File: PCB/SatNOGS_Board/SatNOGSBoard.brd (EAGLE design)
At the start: 58.1 x 68.6 mm, 13 parts

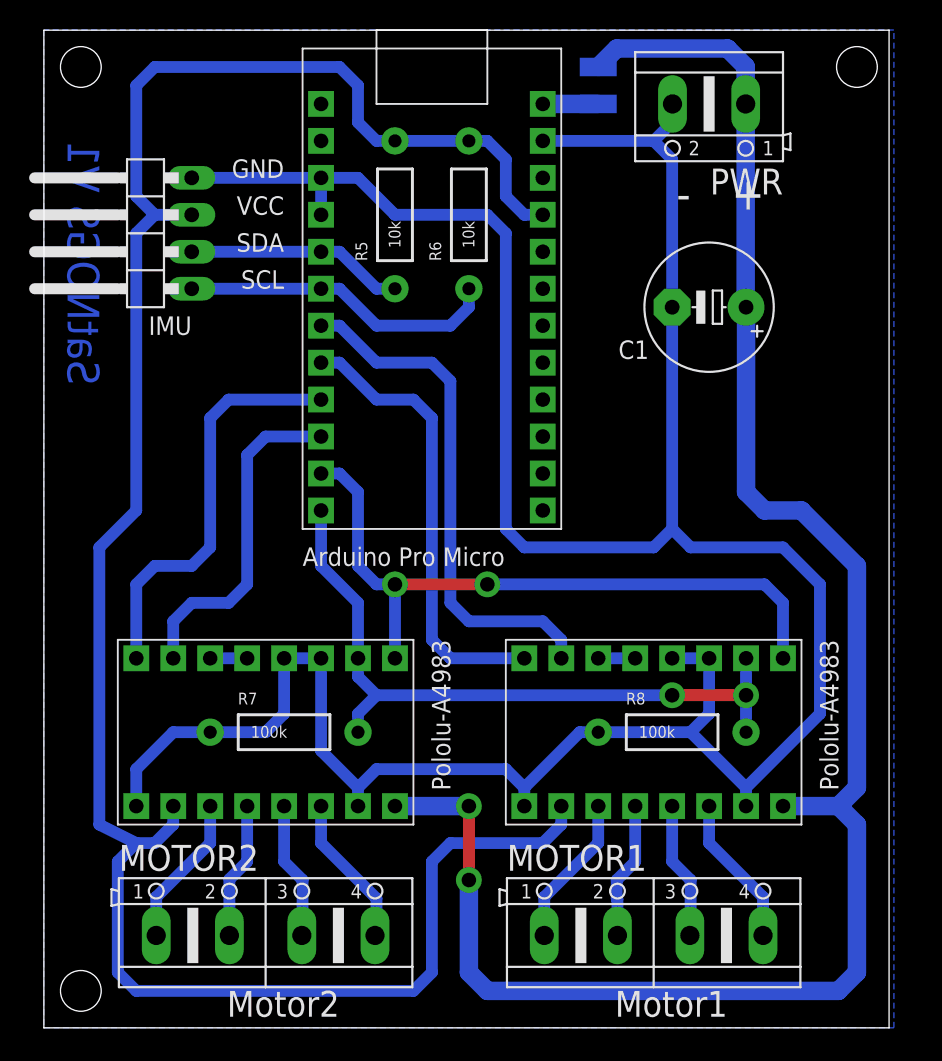
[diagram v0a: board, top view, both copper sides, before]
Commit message: Arduino code with AccelStepper library, add Gerber files for arduino shield, add power supply board.
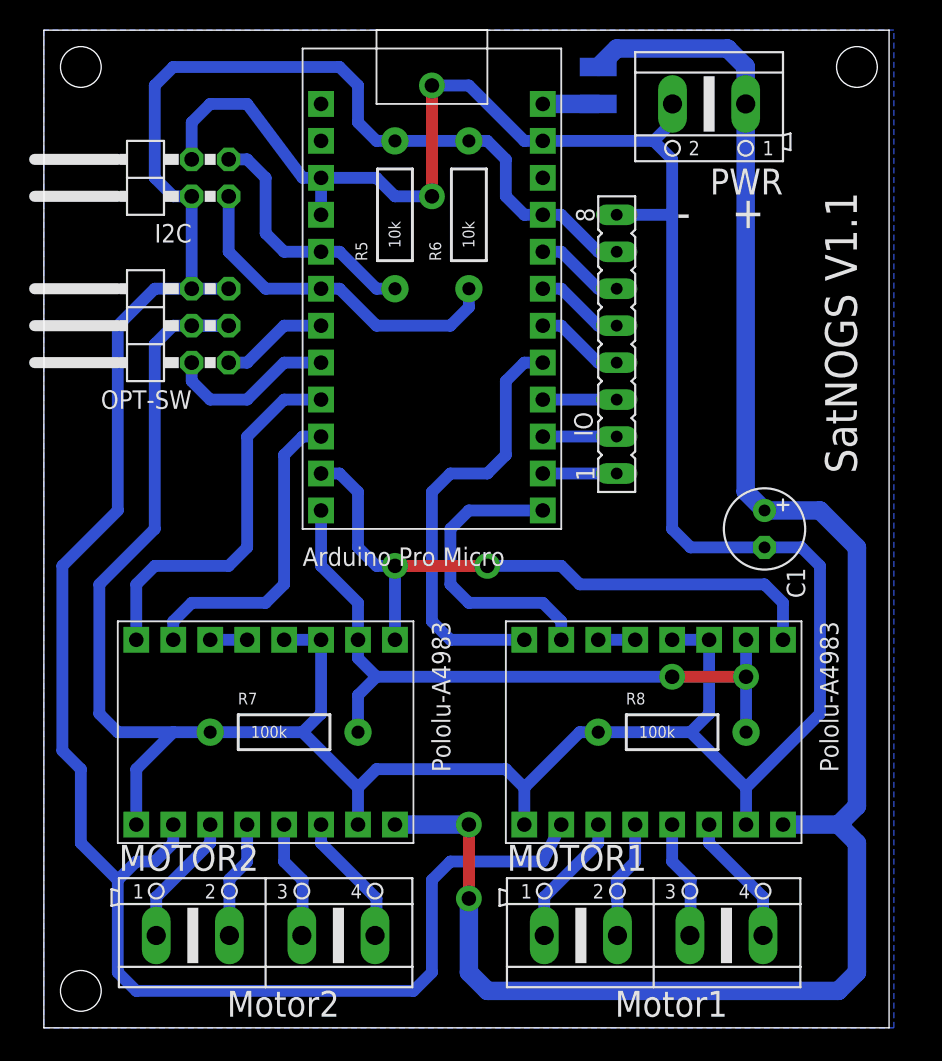
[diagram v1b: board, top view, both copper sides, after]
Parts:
- removed IMU: 10DOF, pinhead:1X04/90
- added I2C: 1, pinhead:2X02/90
- added IO: 1, con-lsta:FE08
- added OPT-SW: 1, pinhead:2X03/90
- C1: value 1000u -> 100uF; device rcl:E5-8,5 -> rcl:E2,5-6
- MOTOR1: value con2 -> 2
- MOTOR2: value con3 -> 3
- PWR: value con1 -> 1
- moved C1 15.7 mm to (49.5, 34.3), turned to 270 degrees
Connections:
- new net IO1: IO.6, UC.20
- new net IO2: IO.5, UC.19
- new net IO3: IO.4, UC.18
- new net IO4: IO.3, UC.16
- new net IO5: IO.2, UC.15
- new net IO6: IO.1, UC.14
- new net SW1: OPT-SW.1, UC.7
- new net SW2: OPT-SW.2, UC.8
- net DIR-1: now also UC.17; no longer UC.8
- net GND: now also I2C.4, IO.8, OPT-SW.3, OPT-SW.4; no longer IMU.4
- net SCL: now also I2C.1; no longer IMU.1
- net SDA: now also I2C.3; no longer IMU.2
- net STEP-1: now also UC.13; no longer UC.7
- net VCC: now also I2C.2, IO.7, OPT-SW.5, OPT-SW.6; no longer IMU.3
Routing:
- net GND: track 197.6 -> 232.0 mm, vias 0 -> 2
- net STEP-1: track 35.7 -> 20.6 mm
- net SW2: track 0.00 -> 11.7 mm
- net VCC: track 149.2 -> 158.7 mm
- net SW1: track 0.00 -> 7.40 mm
- net IO1: track 0.00 -> 6.13 mm
- net IO3: track 0.00 -> 6.13 mm
- net IO2: track 0.00 -> 6.13 mm
- net IO6: track 0.00 -> 5.08 mm
- net IO5: track 0.00 -> 5.08 mm
- net IO4: track 0.00 -> 5.08 mm
- net SCL: track 21.9 -> 24.2 mm
- net SDA: track 15.0 -> 17.3 mm
- net M_EN: track 47.3 -> 45.3 mm
- net DIR-2: track 28.2 -> 26.2 mm
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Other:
- board text added: "SatNOGS V1.1"
- board text removed: "GND"
- board text removed: "SCL"
- board text removed: "SDA"
- board text removed: "SatNOGS V1"
- board text removed: "VCC"

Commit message: Add new components in SatNOGS Board and update Gerber files.
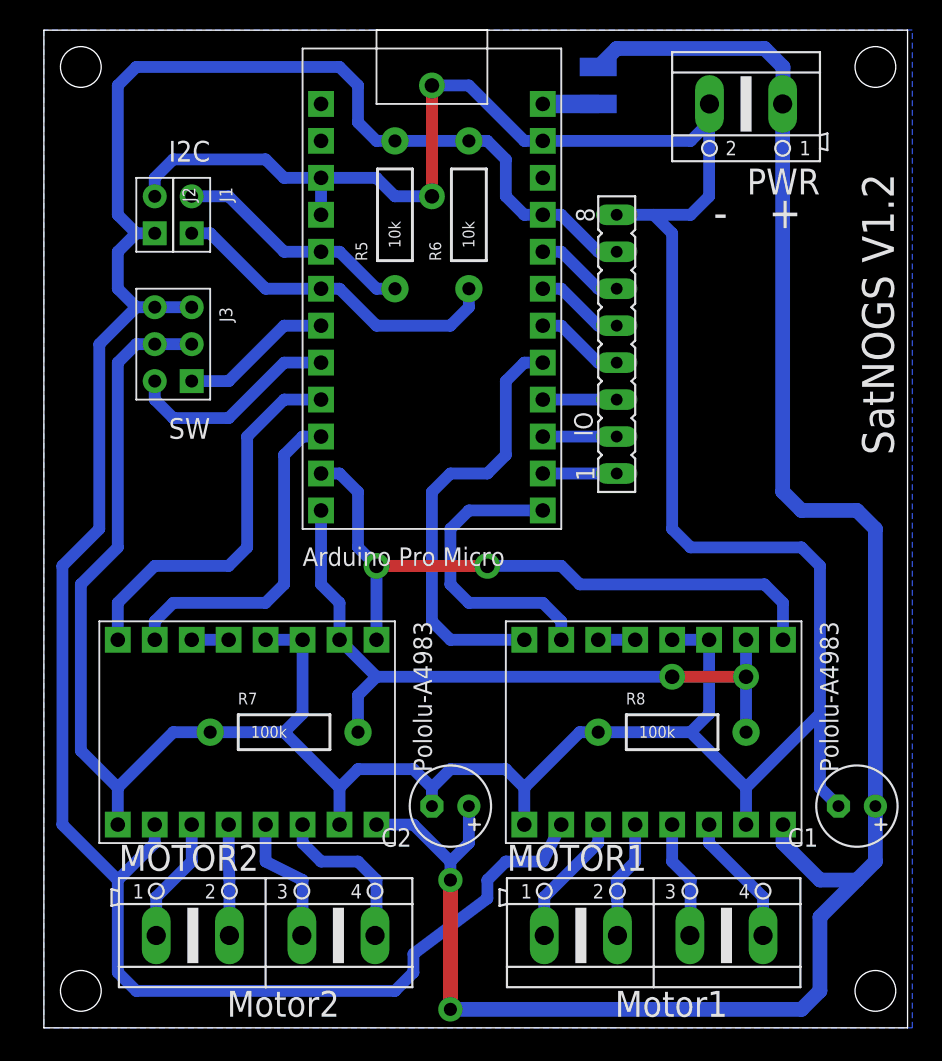
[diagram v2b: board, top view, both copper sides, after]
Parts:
- removed I2C: 1, pinhead:2X02/90
- removed OPT-SW: 1, pinhead:2X03/90
- added C2: 100uF, rcl:E2,5-6
- added J1: 2, Connector:2P-2.54-65/35MIL
- added J2: 3, Connector:2P-2.54-65/35MIL
- added J3: 4, Connector:2X3P-2.54-65/35MIL
- moved C1 20.1 mm to (55.9, 15.2), turned to 180 degrees
- moved PWR 2.54 mm to (48.3, 63.5)
- moved DRIVER2 1.27 mm to (14.0, 20.3)
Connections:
- net GND: now also C2.-, J2.2, J3.2, J3.5; no longer I2C.4, OPT-SW.3, OPT-SW.4
- net SCL: now also J1.1; no longer I2C.1
- net SDA: now also J1.2; no longer I2C.3
- net SW1: now also J3.1; no longer OPT-SW.1
- net SW2: now also J3.6; no longer OPT-SW.2
- net VCC: now also J2.1, J3.3, J3.4; no longer I2C.2, OPT-SW.5, OPT-SW.6
- net VMOTOR: now also C2.+
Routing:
- net VMOTOR: track 126.7 -> 137.7 mm
- net GND: track 232.0 -> 242.8 mm
- net SW2: track 11.7 -> 14.8 mm
- net SW1: track 7.40 -> 10.5 mm
- net VCC: track 158.7 -> 156.7 mm
- net 2-2B: track 9.24 -> 11.3 mm
- net STEP-2: track 21.9 -> 23.2 mm
- net 2-2A: track 8.17 -> 9.21 mm
- net SCL: track 24.2 -> 23.5 mm
- net SDA: track 17.3 -> 16.6 mm
- net DIR-2: track 26.2 -> 26.8 mm
- net 2-1B: track 9.16 -> 8.63 mm
- net 2-1A: track 8.13 -> 7.62 mm
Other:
- board size 58.1 x 68.6 mm -> 59.4 x 68.6 mm
- board text added: "I2C"
- board text added: "SW"
- board text added: "SatNOGS V1.2"
- board text removed: "SatNOGS V1.1"
